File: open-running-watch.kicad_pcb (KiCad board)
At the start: 4 copper layers, 0 parts

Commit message: Place all components to PCB; Defined board layout
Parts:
- added AC1: LIS2DE12TR, LIS2DE12TR:LIS2DE12TR, F.Cu at (248.6, 113.5)
- added ANT1: WLA.04, WLA.04:WLA04, F.Cu at (225.0, 108.8)
- added ANT2: PCS.55.A, PCS.55.A:PCS55A, F.Cu at (240.0, 59.6)
- added BT1: Battery, Connector_Wire:SolderWire-0.1sqmm_1x02_P3.6mm_D0.4mm_OD1mm_Relief, F.Cu at (191.2, 94.1)
- added C1: 100n, Capacitor_SMD:C_0402_1005Metric, F.Cu at (211.6, 93.3)
- added C10: 24p, Capacitor_SMD:C_0402_1005Metric, F.Cu at (214.5, 93.3)
- added C11: 24p, Capacitor_SMD:C_0402_1005Metric, F.Cu at (214.5, 95.3)
- added C12: 24p, Capacitor_SMD:C_0402_1005Metric, F.Cu at (214.5, 97.2)
- added C13: 0.5p, Capacitor_SMD:C_0402_1005Metric, F.Cu at (214.5, 99.2)
- added C14: 0.4p, Capacitor_SMD:C_0402_1005Metric, F.Cu at (214.5, 101.2)
- added C16: 2.2p, Capacitor_SMD:C_0402_1005Metric, F.Cu at (238.3, 67.1)
- added C17: 100n, Capacitor_SMD:C_0402_1005Metric, F.Cu at (238.3, 69.1)
- added C18: 100n, Capacitor_SMD:C_0402_1005Metric, F.Cu at (238.3, 71.0)
- added C19: 120p, Capacitor_SMD:C_0402_1005Metric, F.Cu at (238.3, 73.0)
- added C2: 1u, Capacitor_SMD:C_0603_1608Metric, F.Cu at (220.8, 93.6)
- added C20: 1n, Capacitor_SMD:C_0402_1005Metric, F.Cu at (238.3, 75.0)
- added C21: 120p, Capacitor_SMD:C_0402_1005Metric, F.Cu at (238.3, 77.0)
- added C22: 1u, Capacitor_SMD:C_0603_1608Metric, F.Cu at (187.4, 93.6)
- added C23: 1u, Capacitor_SMD:C_0603_1608Metric, F.Cu at (187.4, 96.1)
- added C24: 1u, Capacitor_SMD:C_0603_1608Metric, F.Cu at (187.4, 98.6)
- added C25: 1u, Capacitor_SMD:C_0603_1608Metric, F.Cu at (187.4, 101.1)
- added C26: 4.7u, Capacitor_SMD:C_0402_1005Metric, F.Cu at (202.2, 102.9)
- added C27: 4.7u, Capacitor_SMD:C_0402_1005Metric, F.Cu at (202.2, 104.9)
- added C28: 4.7u, Capacitor_SMD:C_0402_1005Metric, F.Cu at (202.2, 106.8)
- added C29: 2.2u, Capacitor_SMD:C_0402_1005Metric, F.Cu at (202.2, 108.8)
- added C3: 100n, Capacitor_SMD:C_0402_1005Metric, F.Cu at (211.6, 95.3)
- added C30: 2.2u, Capacitor_SMD:C_0402_1005Metric, F.Cu at (202.2, 110.8)
- added C31: 4.7u, Capacitor_SMD:C_0402_1005Metric, F.Cu at (202.2, 112.8)
- added C32: 1u, Capacitor_SMD:C_0603_1608Metric, F.Cu at (225.1, 121.5)
- added C33: 1u, Capacitor_SMD:C_0603_1608Metric, F.Cu at (225.1, 124.0)
- added C34: 100n, Capacitor_SMD:C_0402_1005Metric, F.Cu at (222.2, 113.4)
- added C35: 100n, Capacitor_SMD:C_0402_1005Metric, F.Cu at (222.2, 115.4)
- added C36: 100n, Capacitor_SMD:C_0402_1005Metric, F.Cu at (222.2, 117.4)
- added C37: 1u, Capacitor_SMD:C_0603_1608Metric, F.Cu at (225.1, 126.5)
- added C38: 100n, Capacitor_SMD:C_0402_1005Metric, F.Cu at (252.6, 117.0)
- added C39: 100n, Capacitor_SMD:C_0402_1005Metric, F.Cu at (252.6, 118.9)
- added C4: 1u, Capacitor_SMD:C_0603_1608Metric, F.Cu at (220.8, 96.1)
- added C40: 1u, Capacitor_SMD:C_0603_1608Metric, F.Cu at (253.2, 112.2)
- added C41: 1u, Capacitor_SMD:C_0603_1608Metric, F.Cu at (253.2, 114.7)
- added C42: 100n, Capacitor_SMD:C_0402_1005Metric, F.Cu at (257.8, 86.1)
- added C43: 100n, Capacitor_SMD:C_0402_1005Metric, F.Cu at (210.0, 54.0)
- added C44: 100n, Capacitor_SMD:C_0402_1005Metric, F.Cu at (210.0, 56.0)
- added C45: 100n, Capacitor_SMD:C_0402_1005Metric, F.Cu at (210.0, 58.0)
- added C46: 100n, Capacitor_SMD:C_0402_1005Metric, F.Cu at (210.0, 59.9)
- added C47: 1u, Capacitor_SMD:C_0603_1608Metric, F.Cu at (196.1, 68.8)
- added C48: 1u, Capacitor_SMD:C_0603_1608Metric, F.Cu at (196.1, 71.3)
- added C49: 1u, Capacitor_SMD:C_0603_1608Metric, F.Cu at (196.1, 73.8)
- added C5: 100n, Capacitor_SMD:C_0402_1005Metric, F.Cu at (211.6, 97.2)
- added C50: 1u, Capacitor_SMD:C_0603_1608Metric, F.Cu at (196.1, 76.3)
- added C51: 100n, Capacitor_SMD:C_0402_1005Metric, F.Cu at (210.0, 61.9)
- added C52: 100n, Capacitor_SMD:C_0402_1005Metric, F.Cu at (210.0, 63.9)
- added C53: 100n, Capacitor_SMD:C_0402_1005Metric, F.Cu at (212.9, 54.0)
- added C54: 100n, Capacitor_SMD:C_0402_1005Metric, F.Cu at (212.9, 56.0)
- added C55: 100n, Capacitor_SMD:C_0402_1005Metric, F.Cu at (212.9, 58.0)
- added C56: 1u, Capacitor_SMD:C_0603_1608Metric, F.Cu at (196.1, 78.8)
- added C57: 1u, Capacitor_SMD:C_0603_1608Metric, F.Cu at (196.1, 81.3)
- added C58: 1u, Capacitor_SMD:C_0603_1608Metric, F.Cu at (196.1, 83.8)
- added C59: 1u, Capacitor_SMD:C_0603_1608Metric, F.Cu at (196.1, 86.3)
- added C6: 24p, Capacitor_SMD:C_0402_1005Metric, F.Cu at (211.6, 99.2)
- added C60: 1u, Capacitor_SMD:C_0603_1608Metric, F.Cu at (196.1, 88.9)
- added C61: 3.3p, Capacitor_SMD:C_0402_1005Metric, F.Cu at (212.9, 59.9)
- added C62: 3.3p, Capacitor_SMD:C_0402_1005Metric, F.Cu at (212.9, 61.9)
- added C63: 4.7u, Capacitor_SMD:C_0402_1005Metric, F.Cu at (202.2, 114.7)
- added C64: 10u, Capacitor_SMD:C_0603_1608Metric, F.Cu at (187.4, 103.6)
- added C65: 10u, Capacitor_SMD:C_0603_1608Metric, F.Cu at (187.4, 106.1)
- added C66: 10u, Capacitor_SMD:C_0603_1608Metric, F.Cu at (187.4, 108.6)
- added C7: 100n, Capacitor_SMD:C_0402_1005Metric, F.Cu at (211.6, 101.2)
- added C72: 100n, Capacitor_SMD:C_0402_1005Metric, F.Cu at (202.9, 118.7)
- added C73: 100n, Capacitor_SMD:C_0402_1005Metric, F.Cu at (192.4, 118.7)
- added C74: 100n, Capacitor_SMD:C_0402_1005Metric, F.Cu at (252.9, 81.0)
- added C75: 100n, Capacitor_SMD:C_0402_1005Metric, F.Cu at (253.1, 122.9)
- added C77: 100n, Capacitor_SMD:C_0402_1005Metric, F.Cu at (232.0, 81.0)
- added C78: 100n, Capacitor_SMD:C_0402_1005Metric, F.Cu at (258.7, 93.3)
- added C79: 1u, Capacitor_SMD:C_0603_1608Metric, F.Cu at (233.4, 100.2)
- added C8: 1u, Capacitor_SMD:C_0603_1608Metric, F.Cu at (220.8, 98.6)
- added C80: 100n, Capacitor_SMD:C_0402_1005Metric, F.Cu at (247.1, 93.3)
- added C81: 100n, Capacitor_SMD:C_0402_1005Metric, F.Cu at (247.1, 95.3)
- added C82: 1u, Capacitor_SMD:C_0603_1608Metric, F.Cu at (233.4, 102.7)
- added C83: 100n, Capacitor_SMD:C_0402_1005Metric, F.Cu at (242.4, 81.0)
- added C84: 560p, Capacitor_SMD:C_0402_1005Metric, F.Cu at (247.1, 97.2)
- added C85: 1u, Capacitor_SMD:C_0603_1608Metric, F.Cu at (233.4, 105.2)
- added C86: 1u, Capacitor_SMD:C_0603_1608Metric, F.Cu at (233.4, 107.7)
- added C9: 100n, Capacitor_SMD:C_0402_1005Metric, F.Cu at (211.6, 103.2)
- added D1: BAS16LT3G, BAS16LT3G:SOT96P237X111-3N, F.Cu at (233.9, 124.3)
- added FL1: B39162B4327P810, B39162B4327P810:FIL_B39162B4327P810, F.Cu at (244.6, 67.5)
- added IC1: BLUENRG-232N, BLUENRG-232N:QFN50P500X500X100-33N-D, F.Cu at (222.5, 103.5)
- added IC10: NXB0108BQX, NXB0108BQX:NXB0108BQX, F.Cu at (218.6, 56.4)
- added IC11: STM32L475RGT6, STM32L475RGT6:QFP50P1200X1200X160-64N, F.Cu at (201.3, 60.3)
- added IC12: W25N512GVEIG, W25N512GVEIG:SON127P800X600X80-9N-D, F.Cu at (215.7, 71.3)
- added IC13: TPS613222ADBVR, TPS613222ADBVR:SOT95P280X145-5N, F.Cu at (199.3, 94.6)
- added IC14: INA186A5IYFDR, INA186A5IYFDR:BGA6C40P3X2_117X76X40, F.Cu at (202.5, 122.4)
- added IC15: INA186A5IYFDR, INA186A5IYFDR:BGA6C40P3X2_117X76X40, F.Cu at (192.1, 122.4)
- added IC16: INA186A5IYFDR, INA186A5IYFDR:BGA6C40P3X2_117X76X40, F.Cu at (252.6, 84.7)
- added IC17: INA186A5IYFDR, INA186A5IYFDR:BGA6C40P3X2_117X76X40, F.Cu at (252.8, 126.6)
- added IC19: INA186A5IYFDR, INA186A5IYFDR:BGA6C40P3X2_117X76X40, F.Cu at (231.6, 84.7)
- added IC2: TESEO-LIV3F, TESEO-LIV3F:SON110P970X1010X230-18N, F.Cu at (230.9, 72.2)
- added IC20: INA186A5IYFDR, INA186A5IYFDR:BGA6C40P3X2_117X76X40, F.Cu at (258.4, 97.0)
- added IC21: LSF0204GU12X, LSF0204GU12X:LSF0204GU12X, F.Cu at (243.1, 95.0)
- added IC22: INA186A5IYFDR, INA186A5IYFDR:BGA6C40P3X2_117X76X40, F.Cu at (242.1, 84.7)
- added IC3: BGA_725L6_E6327, BGA_725L6_E6327:BGA725L6E6327, F.Cu at (244.3, 70.2)
- added IC4: BQ27441DRZR-G1A, BQ27441DRZR-G1A:BQ27441DRZRG1A, F.Cu at (197.5, 105.9)
- added IC5: MCP73811T-420I_OT, MCP73811T-420I_OT:SOT95P270X145-5N, F.Cu at (197.1, 112.5)
- added IC6: TPS62237DRYR, TPS62237DRYR:TPS62237DRYR, F.Cu at (198.7, 99.2)
- added IC7: ST1S15J18R, ST1S15J18R:BGA6C40P2X3_94X119X60, F.Cu at (203.9, 97.7)
- added IC8: TLV9002SIRUGR, TLV9002SIRUGR:QFN50P150X200X40-10N, F.Cu at (225.5, 114.7)
- added IC9: ICP-10100, ICP-10100:ICP10100, F.Cu at (258.9, 82.6)
- added J1: 20021121-00014T4LF, 20021121-00014T4LF:2002112100014T4LF, F.Cu at (204.1, 81.3)
- added J2: 10118192-0001LF, 10118192-0001LF:101181920001LF, F.Cu at (204.3, 72.1)
- added J5: 1-2328702-0, 1-2328702-0:123287020, F.Cu at (236.0, 95.6)
- added J6: 2328702-4, 2328702-4:23287024, F.Cu at (238.5, 103.4)
- added L1: 10u, Inductor_SMD:L_0805_2012Metric, F.Cu at (221.1, 108.5)
- added L2: 10n, Inductor_SMD:L_0402_1005Metric, F.Cu at (241.2, 67.1)
- added L3: 5.6n, Inductor_SMD:L_0402_1005Metric, F.Cu at (241.2, 69.1)
- added L4: 1u, Inductor_SMD:L_1008_2520Metric, F.Cu at (191.9, 103.8)
- added L5: 1u, Inductor_SMD:L_1008_2520Metric, F.Cu at (191.9, 107.5)
- added L6: 470n, Inductor_SMD:L_0805_2012Metric, F.Cu at (205.9, 113.2)
- added L7: 2.2u, Inductor_SMD:L_1008_2520Metric, F.Cu at (191.9, 111.3)
- added L8: 15n, Inductor_SMD:L_0402_1005Metric, F.Cu at (241.2, 71.1)
- added LED1: SFH_7072, SFH_7072:SFH7072, F.Cu at (215.5, 116.3)
- added LS1: CMT-7525-80-SMT-TR, CMT-7525-80-SMT-TR:CMT752580SMTTR, F.Cu at (236.9, 116.5)
- added Q1: BC847BS, Package_TO_SOT_SMD:SOT-363_SC-70-6, F.Cu at (221.0, 122.2)
- added Q2: BC847BS, Package_TO_SOT_SMD:SOT-363_SC-70-6, F.Cu at (221.0, 126.1)
- added Q3: BC817-25-QVL, BC817-25-QVL:SOT95P230X110-3N, F.Cu at (238.8, 124.3)
- added Q4: BC847, Package_TO_SOT_SMD:SOT-23, F.Cu at (247.2, 101.3)
- added R1: 10k, Resistor_SMD:R_0402_1005Metric, F.Cu at (217.3, 93.3)
- added R10: 10k, Resistor_SMD:R_0402_1005Metric, F.Cu at (205.1, 108.9)
- added R11: 10k, Resistor_SMD:R_0402_1005Metric, F.Cu at (205.1, 110.9)
- added R12: 1.5M, Resistor_SMD:R_0402_1005Metric, F.Cu at (211.6, 121.2)
- added R13: 100k, Resistor_SMD:R_0402_1005Metric, F.Cu at (211.6, 123.2)
- added R14: 47, Resistor_SMD:R_0402_1005Metric, F.Cu at (211.6, 125.2)
- added R15: 10k, Resistor_SMD:R_0402_1005Metric, F.Cu at (211.6, 127.2)
- added R16: 100, Resistor_SMD:R_0402_1005Metric, F.Cu at (211.6, 129.2)
- added R17: 10k, Resistor_SMD:R_0402_1005Metric, F.Cu at (214.5, 121.2)
- added R18: 1.5M, Resistor_SMD:R_0402_1005Metric, F.Cu at (214.5, 123.2)
- added R19: 10k, Resistor_SMD:R_0402_1005Metric, F.Cu at (214.5, 125.2)
- added R2: 10k, Resistor_SMD:R_0402_1005Metric, F.Cu at (217.3, 95.3)
- added R20: 10k, Resistor_SMD:R_0402_1005Metric, F.Cu at (214.5, 127.2)
- added R21: 1.5M, Resistor_SMD:R_0402_1005Metric, F.Cu at (214.5, 129.2)
- added R22: 47, Resistor_SMD:R_0402_1005Metric, F.Cu at (217.4, 121.2)
- added R23: 75, Resistor_SMD:R_0402_1005Metric, F.Cu at (217.4, 123.2)
- added R24: 10k, Resistor_SMD:R_0402_1005Metric, F.Cu at (217.4, 125.2)
- added R25: 10k, Resistor_SMD:R_0402_1005Metric, F.Cu at (217.4, 127.2)
- added R26: 10k, Resistor_SMD:R_0402_1005Metric, F.Cu at (211.5, 85.3)
- added R27: 10k, Resistor_SMD:R_0402_1005Metric, F.Cu at (211.5, 87.3)
- added R28: 10k, Resistor_SMD:R_0402_1005Metric, F.Cu at (211.5, 89.3)
- added R29: 10k, Resistor_SMD:R_0402_1005Metric, F.Cu at (214.4, 85.3)
- added R3: 10k, Resistor_SMD:R_0402_1005Metric, F.Cu at (217.3, 97.3)
- added R30: 10k, Resistor_SMD:R_0402_1005Metric, F.Cu at (214.4, 87.3)
- added R31: 10k, Resistor_SMD:R_0402_1005Metric, F.Cu at (214.4, 89.3)
- added R32: 10k, Resistor_SMD:R_0402_1005Metric, F.Cu at (217.3, 85.3)
- added R33: 10k, Resistor_SMD:R_0402_1005Metric, F.Cu at (217.3, 87.3)
- added R34: 10m, Resistor_SMD:R_1206_3216Metric, F.Cu at (198.7, 119.3)
- added R35: 10k, Resistor_SMD:R_0402_1005Metric, F.Cu at (202.4, 124.8)
- added R36: 0, Resistor_SMD:R_0402_1005Metric_Pad0.72x0.64mm_HandSolder, F.Cu at (197.5, 125.3)
- added R37: 10m, Resistor_SMD:R_1206_3216Metric, F.Cu at (188.2, 119.3)
- added R38: 10k, Resistor_SMD:R_0402_1005Metric, F.Cu at (191.9, 124.8)
- added R39: 0, Resistor_SMD:R_0402_1005Metric_Pad0.72x0.64mm_HandSolder, F.Cu at (187.0, 125.3)
- added R4: 10k, Resistor_SMD:R_0402_1005Metric, F.Cu at (217.3, 99.3)
- added R40: 10m, Resistor_SMD:R_1206_3216Metric, F.Cu at (248.7, 81.7)
- added R41: 10k, Resistor_SMD:R_0402_1005Metric, F.Cu at (252.4, 87.2)
- added R42: 0, Resistor_SMD:R_0402_1005Metric_Pad0.72x0.64mm_HandSolder, F.Cu at (247.5, 87.6)
- added R43: 10m, Resistor_SMD:R_1206_3216Metric, F.Cu at (248.9, 123.6)
- added R44: 10k, Resistor_SMD:R_0402_1005Metric, F.Cu at (252.6, 129.1)
- added R45: 0, Resistor_SMD:R_0402_1005Metric_Pad0.72x0.64mm_HandSolder, F.Cu at (247.7, 129.5)
- added R46: 10k, Resistor_SMD:R_0402_1005Metric, F.Cu at (246.2, 104.5)
- added R47: 10k, Resistor_SMD:R_0402_1005Metric, F.Cu at (217.3, 89.3)
- added R49: 240, Resistor_SMD:R_0402_1005Metric, F.Cu at (242.6, 123.0)
- added R5: 10k, Resistor_SMD:R_0402_1005Metric, F.Cu at (241.2, 73.1)
- added R50: 10m, Resistor_SMD:R_1206_3216Metric, F.Cu at (227.7, 81.7)
- added R51: 10k, Resistor_SMD:R_0402_1005Metric, F.Cu at (231.4, 87.2)
- added R52: 0, Resistor_SMD:R_0402_1005Metric_Pad0.72x0.64mm_HandSolder, F.Cu at (226.5, 87.6)
- added R53: 10m, Resistor_SMD:R_1206_3216Metric, F.Cu at (254.5, 94.0)
- added R54: 10k, Resistor_SMD:R_0402_1005Metric, F.Cu at (258.2, 99.5)
- added R55: 0, Resistor_SMD:R_0402_1005Metric_Pad0.72x0.64mm_HandSolder, F.Cu at (253.3, 99.9)
- added R56: 10m, Resistor_SMD:R_1206_3216Metric, F.Cu at (238.2, 81.7)
- added R57: 10k, Resistor_SMD:R_0402_1005Metric, F.Cu at (241.9, 87.2)
- added R58: 0, Resistor_SMD:R_0402_1005Metric_Pad0.72x0.64mm_HandSolder, F.Cu at (237.0, 87.6)
- added R59: 0, Resistor_SMD:R_0402_1005Metric_Pad0.72x0.64mm_HandSolder, F.Cu at (243.2, 99.9)
- added R6: 10m, Resistor_SMD:R_1206_3216Metric, F.Cu at (204.7, 94.0)
- added R60: 0, Resistor_SMD:R_0402_1005Metric_Pad0.72x0.64mm_HandSolder, F.Cu at (243.2, 101.9)
- added R61: 0, Resistor_SMD:R_0402_1005Metric_Pad0.72x0.64mm_HandSolder, F.Cu at (243.2, 103.9)
- added R62: 0, Resistor_SMD:R_0402_1005Metric_Pad0.72x0.64mm_HandSolder, F.Cu at (243.2, 105.9)
- added R7: 2k, Resistor_SMD:R_0402_1005Metric, F.Cu at (205.1, 102.9)
- added R8: 10k, Resistor_SMD:R_0402_1005Metric, F.Cu at (205.1, 104.9)
- added R9: 1M, Resistor_SMD:R_0402_1005Metric, F.Cu at (205.1, 106.9)
- added S1: RKB2SJM250SMTR_LFS, RKB2SJM250SMTR_LFS:RKB2SJM250SMTRLFS, F.Cu at (218.6, 63.0)
- added S2: JS102011JCQN, JS102011JCQN:JS102011JCQN, F.Cu at (215.9, 80.5)
- added S3: EVQ-P7J01P, EVQ-P7J01P:EVQP7J01P, F.Cu at (189.7, 56.0)
- added S4: EVQ-P7J01P, EVQ-P7J01P:EVQP7J01P, F.Cu at (189.7, 62.0)
- added S5: EVQ-P7J01P, EVQ-P7J01P:EVQP7J01P, F.Cu at (189.7, 68.0)
- added S6: EVQ-P7J01P, EVQ-P7J01P:EVQP7J01P, F.Cu at (189.7, 74.0)
- added S7: EVQ-P7J01P, EVQ-P7J01P:EVQP7J01P, F.Cu at (189.7, 80.0)
- added T1: BALF-NRG-02D3, BALF-NRG-02D3:BALFNRG02D3, F.Cu at (227.9, 101.1)
- added TP1: 5029, 5029:5029, F.Cu at (198.4, 122.6)
- added TP2: 5029, 5029:5029, F.Cu at (187.9, 122.6)
- added TP3: 5029, 5029:5029, F.Cu at (248.4, 85.0)
- added TP4: 5029, 5029:5029, F.Cu at (248.6, 126.8)
- added TP6: 5029, 5029:5029, F.Cu at (227.4, 85.0)
- added TP7: 5029, 5029:5029, F.Cu at (254.2, 97.2)
- added TP8: 5029, 5029:5029, F.Cu at (237.9, 85.0)
- added U1: TPS62233DRYR, Package_SON:Texas_USON-6_1x1.45mm_P0.5mm_SMD, F.Cu at (186.8, 111.6)
- added Y1: ECS-320-12-37B2-7KM-TR, ECS-320:ECS3201237B27KMTR, F.Cu at (212.8, 106.6)
- added Y2: NX3215SA-32.768K-EXS00A-MU00003, NX3215SA:NX3215SA32768KEXS00AMU00003, F.Cu at (226.1, 94.8)
- added Y3: ECS-.327-7-1210-TR, ECS-.327-7-1210-TR:ECS32791210TR, F.Cu at (221.2, 86.0)
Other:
- board outline added: 50 x 50 mm

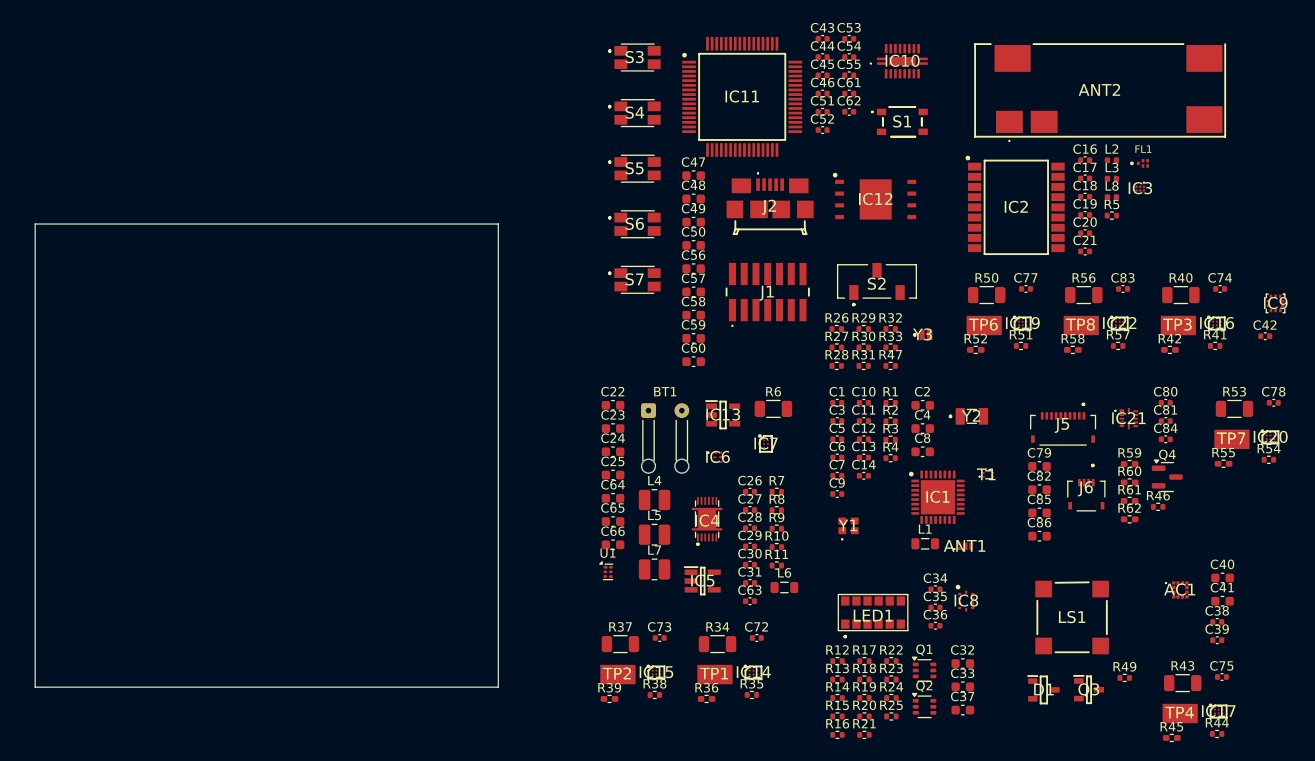
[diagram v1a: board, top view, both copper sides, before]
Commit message: Finished component placement and component grouping wirings
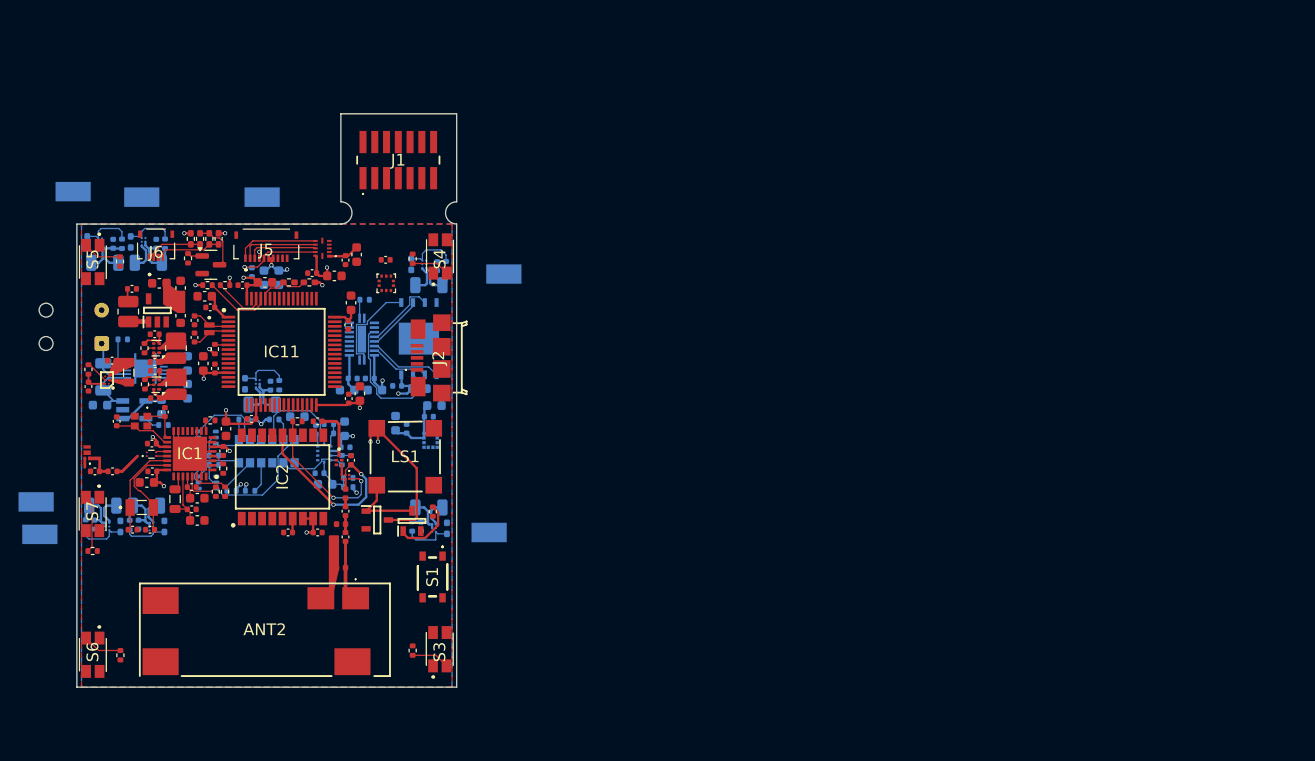
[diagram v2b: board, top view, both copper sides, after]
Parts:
- removed S2: JS102011JCQN, JS102011JCQN:JS102011JCQN
- added R48: 0, Resistor_SMD:R_0402_1005Metric_Pad0.72x0.64mm_HandSolder, F.Cu at (152.4, 80.3)
- added R63: 0, Resistor_SMD:R_0402_1005Metric_Pad0.72x0.64mm_HandSolder, F.Cu at (154.6, 80.3)
- AC1, BT1, C22, C23, C24, C25, C32, C33, C34, C35, C36, C37, C38, C39, C40, C41, C51, C54, C55, C56, C59, C60, C72, C73, C74, C75, C77, C78, C83, C84, C85, C86, IC10, IC12, IC14, IC15, IC16, IC17, IC19, IC20, IC22, IC4, IC5, IC8, LED1, Q1, Q2, R12, R13, R14, R15, R16, R17, R18, R19, R20, R21, R22, R23, R24, R25, R29, R34, R35, R36, R37, R38, R39, R40, R41, R42, R43, R44, R45, R50, R51, R52, R53, R54, R55, R56, R57, R58, R6, R7, R8, TP1, TP2, TP3, TP4, TP6, TP7, TP8: moved to B.Cu
- IC6: footprint TPS62237DRYR:TPS62237DRYR -> Package_SON:Texas_USON-6_1x1.45mm_P0.5mm_SMD
- moved TP3 124.8 mm to (125.1, 104.0), turned to 180 degrees
- moved TP4 124.6 mm to (125.5, 107.5), turned to 180 degrees
- moved R44 124.2 mm to (130.4, 106.5), turned to -90 degrees
- moved C75 122.8 mm to (131.4, 106.5), turned to 90 degrees
- moved IC17 121.6 mm to (132.8, 106.7), turned to -90 degrees
- moved C74 119.5 mm to (136.2, 106.5), turned to 90 degrees
- moved R41 118.8 mm to (135.2, 106.5), turned to -90 degrees
- moved R43 118.1 mm to (132.3, 104.4)
- moved IC16 117.1 mm to (137.5, 106.7), turned to -90 degrees
- moved R45 115.8 mm to (134.2, 106.7), turned to 90 degrees
- moved R40 114.0 mm to (137.0, 104.4)
- moved R42 110.2 mm to (138.9, 106.7), turned to 90 degrees
- moved TP8 109.8 mm to (129.1, 70.5), turned to 180 degrees
- moved IC20 109.5 mm to (149.0, 91.2), turned to 90 degrees
- moved C78 108.3 mm to (150.4, 91.5), turned to -90 degrees
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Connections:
- C64 pad 2: /mip_display/DISP_VDD_IN -> /mip_display/DISP_VDD
- C65 pad 2: /mip_display/DISP_VDD_IN -> /mip_display/DISP_VDD
- C66 pad 2: /mip_display/DISP_VDD_IN -> /mip_display/DISP_VDD
- C79 pad 2: /audio/VCC_IN -> /mip_display/DISP_VDDIO
- C80 pad 2: /audio/VCC_IN -> /mip_display/DISP_VDDIO
- C83 pad 2: /mip_display/DISP_VDD_IN -> /audio/VCC_IN
- IC11 pad 10: /controller/ADC_IN_3 -> /biometric/OUT_IR_EN
- IC11 pad 11: /controller/ADC_IN_4 -> /bluenrg/RESET_N
- IC11 pad 14: unconnected-(IC11-PA0-Pad14) -> /bluenrg/SPI_IRQ
- IC11 pad 15: unconnected-(IC11-PA1-Pad15) -> /biometric/IN_IR
- IC11 pad 2: unconnected-(IC11-PC13-Pad2) -> /biometric/OUT_RG_EN
- IC11 pad 20: unconnected-(IC11-PA4-Pad20) -> /controller/GPS_RESET_N
- IC11 pad 24: unconnected-(IC11-PC4-Pad24) -> /controller/GPS_WAKEUP
- IC11 pad 25: unconnected-(IC11-PC5-Pad25) -> /biometric/IN_G1
- IC11 pad 28: unconnected-(IC11-PB2-Pad28) -> /biometric/IN_G2
- IC11 pad 33: unconnected-(IC11-PB12-Pad33) -> /biometric/IN_R
- IC11 pad 39: unconnected-(IC11-PC8-Pad39) -> /audio/IN
- IC11 pad 41: unconnected-(IC11-PA8-Pad41) -> /accelerometer/INT_2
- IC11 pad 50: unconnected-(IC11-PA15_(JTDI)-Pad50) -> /controller/TIM2_CH1
- IC11 pad 53: /controller/CS3_2 -> /controller/DISP_EN
- IC11 pad 58: unconnected-(IC11-PB6-Pad58) -> /controller/DISP_IO_EN
- IC11 pad 59: unconnected-(IC11-PB7-Pad59) -> /accelerometer/INT_1
- IC13 pad 4: /mip_display/DISP_VDD_IN -> /mip_display/DISP_VDD
- IC2 pad 5: /gps/WAKE_UP -> /controller/GPS_WAKEUP
- IC2 pad 9: /gps/RESET_N -> /controller/GPS_RESET_N
- IC21 pad 11: /audio/VCC_IN -> /mip_display/DISP_VDDIO
- IC21 pad 12: /mip_display/MCU_IO_EN -> /controller/DISP_IO_EN
- IC21 pad 2: /mip_display/MCU_DISP_EN -> /controller/DISP_EN
- IC21 pad 3: /mip_display/MCU_CS -> /controller/CS3_1
- IC21 pad 4: /mip_display/MCU_SDI -> /controller/SPI3_MOSI
- IC21 pad 5: /mip_display/MCU_SCLK -> /controller/SPI3_CK
- IC22 pad A1: /mip_display/DISP_VDD_IN -> /audio/VCC_IN
- IC22 pad A2: /mip_display/DISP_VDD_IN -> /audio/VCC_IN
- IC22 pad B1: /mip_display/DISP_VDD -> /mip_display/DISP_VDDIO
- J1 pad 8: /controller/SWO -> unconnected-(J1-Pad8)
- R46 pad 2: /mip_display/DISP_BRIGHT -> /controller/TIM2_CH1
- R56 pad 1: /mip_display/DISP_VDD_IN -> /audio/VCC_IN
- R56 pad 2: /mip_display/DISP_VDD -> /mip_display/DISP_VDDIO
- R57 pad 1: /mip_display/DISP_VDD_IN -> /audio/VCC_IN
- R60 pad 1: /audio/VCC_IN -> /mip_display/DISP_VDDIO
- R62 pad 2: /audio/VCC_IN -> /mip_display/DISP_VDDIO
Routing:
- net /accelerometer/1V8: track 0.00 -> 33.0 mm
- net /controller/VDD: track 0.00 -> 30.6 mm, vias 0 -> 8
- net /audio/VCC: track 0.00 -> 20.9 mm, vias 0 -> 2
- net /gps/VCC_RF: track 0.00 -> 19.2 mm, vias 0 -> 2
- net /power/SRN: track 0.00 -> 17.9 mm
- net GND: track 0.00 -> 17.4 mm, vias 0 -> 1
- net /gps/ANT_OFF: track 0.00 -> 16.1 mm, vias 0 -> 2
- net /controller/FLASH_IO3: track 0.00 -> 14.5 mm
- net /biometric/VCC_IN: track 0.00 -> 14.3 mm
- net /audio/VCC_IN: track 0.00 -> 12.8 mm
- net /biometric/G2C: track 0.00 -> 12.7 mm
- net /controller/VCC_FLASH: track 0.00 -> 12.6 mm, vias 0 -> 2
- net /biometric/VCC: track 0.00 -> 11.9 mm, vias 0 -> 5
- net /bluenrg/VBAT: track 0.00 -> 11.2 mm, vias 0 -> 3
- net /biometric/PD_IR: track 0.00 -> 11.0 mm
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- added copper zone on In2.Cu, net /audio/VCC
- added copper zone on In2.Cu, net /biometric/VCC
- added copper zone on In2.Cu, net /bluenrg/VBAT
- added copper zone on In2.Cu, net /controller/VCC_FLASH
- added copper zone on In2.Cu, net /controller/VDD
- added copper zone on In2.Cu, net /gps/VCC
- added copper zone on In2.Cu, net /mip_display/DISP_VDD
- added copper zone on In2.Cu, net /mip_display/DISP_VDDIO
- added copper zone on B.Cu, net GND
- added copper zone on F.Cu, net GND
- added copper zone on In1.Cu, net GND
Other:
- board size 50 x 50 mm -> 41 x 61.9 mm

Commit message: Finished hardware design
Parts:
- removed J5: 1-2328702-0, 1-2328702-0:123287020
- removed J6: 2328702-4, 2328702-4:23287024
- added IC18: PCAL9538ABSHP, PCAL9538ABSHP:QFN50P300X300X100-17N-D, B.Cu at (151.1, 83.5)
- added J3: 1-2328702-0, 1-2328702-0:123287020, F.Cu at (149.9, 76.8)
- added J4: 2328702-4, 2328702-4:23287024, F.Cu at (138.4, 76.2)
- added REF**: OSHW-Logo_5.7x6mm_SilkScreen, Symbol:OSHW-Logo_5.7x6mm_SilkScreen, F.Cu at (162.2, 87.6)
- moved TP8 15.1 mm to (143.3, 75.5)
- moved TP7 15.0 mm to (140.2, 82.8)
- moved TP3 11.9 mm to (132.1, 113.6)
- moved TP2 10.1 mm to (132.7, 80.5)
- moved C78 9.78 mm to (145.4, 83.0)
- moved R55 9.78 mm to (142.7, 82.8)
- moved IC20 9.78 mm to (144.1, 82.8)
- moved R53 9.78 mm to (144.6, 85.1)
- moved R54 9.78 mm to (146.4, 83.0)
- moved TP1 8.41 mm to (168.0, 75.8)
- moved TP4 7.38 mm to (132.1, 110.8), turned to 0 degrees
- moved TP6 6.08 mm to (168.6, 110.1), turned to -90 degrees
- moved C86 4.90 mm to (148.3, 75.9), turned to -90 degrees
- moved C85 4.03 mm to (150.8, 75.9), turned to -90 degrees
- moved C84 1.80 mm to (150.2, 79.2)
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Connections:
- C53 pad 1: /accelerometer/1V8 -> /controller/VDD
- C58 pad 1: /accelerometer/1V8 -> /controller/VDD
- IC11 pad 1: /accelerometer/1V8 -> /controller/VDD
- IC11 pad 15: /biometric/IN_IR -> /bluenrg/SPI_CS
- IC11 pad 2: /biometric/OUT_RG_EN -> /controller/BTN_INT
- IC11 pad 25: /biometric/IN_G1 -> /biometric/IN_G2
- IC11 pad 28: /biometric/IN_G2 -> /biometric/IN_IR
- IC11 pad 38: /bluenrg/SPI_CS -> /biometric/IN_G1
- IC12 pad 9: unconnected-(IC12-EP-Pad9) -> GND
- IC8 pad 2: /biometric/OUT_RG_EN -> /biometric/OUT_IR_EN
- J1 pad 3: /controller/VDD -> /accelerometer/1V8
- R30 pad 2: /controller/VDD -> /accelerometer/1V8
- R31 pad 2: /controller/VDD -> /accelerometer/1V8
- R32 pad 2: /controller/VDD -> /accelerometer/1V8
- R33 pad 2: /controller/VDD -> /accelerometer/1V8
- R47 pad 2: /controller/VDD -> /accelerometer/1V8
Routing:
- net /accelerometer/1V8: track 33.0 -> 225.6 mm, vias 0 -> 13
- net /controller/NRST: track 1.49 -> 99.3 mm, vias 0 -> 3
- net /barometer/SDA: track 5.67 -> 87.1 mm, vias 0 -> 2
- net /barometer/SCL: track 7.20 -> 77.2 mm, vias 0 -> 1
- net Net-(IC18-P1): track 4.12 -> 73.5 mm, vias 0 -> 1
- net /biometric/VCC_IN: track 14.3 -> 77.4 mm, vias 0 -> 4
- net Net-(IC18-P5): track 4.26 -> 63.0 mm, vias 0 -> 3
- net /audio/VCC_IN: track 12.8 -> 67.7 mm, vias 0 -> 3
- net /accelerometer/INT_1: track 0.00 -> 52.9 mm, vias 0 -> 6
- net /biometric/IN_G1: track 0.00 -> 48.2 mm, vias 0 -> 3
- net /biometric/OUT_IR_EN: track 0.00 -> 46.0 mm, vias 0 -> 3
- net Net-(IC18-P4): track 6.26 -> 51.1 mm, vias 0 -> 3
- net /accelerometer/SPC: track 0.00 -> 43.1 mm, vias 0 -> 3
- net /accelerometer/SDO: track 0.00 -> 42.4 mm, vias 0 -> 1
- net /biometric/IN_R: track 0.00 -> 42.3 mm, vias 0 -> 3
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- added copper zone on In2.Cu, net /power/SRN
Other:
- board text added: "+"
- board text added: "1"
- board text added: "1V8"
- board text added: "GND"
- board text added: "NRST"
- board text added: "RX"
- board text added: "SWCLK"
- board text added: "SWDIO"
- board text added: "TX"
- board text added: "github.com/fuad1502/open-running-watch-hw"
- board text added: "v0.1.0"

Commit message: Pulled in symbol attribute changes from schematic to PCB
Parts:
- renumbered REF** to LOGO1
